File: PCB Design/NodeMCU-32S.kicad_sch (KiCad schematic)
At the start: 23 parts, among them J1 Screw_Terminal_01x02, J2 Screw_Terminal_01x02, J3 Screw_Terminal_01x02, J4 Screw_Terminal_01x02, J5 Screw_Terminal_01x03, J6 Screw_Terminal_01x02, Q1 IRLZ44N, Q2 2N2646, SW1 SW_DPDT_x2, U1 ESP32-DevKitC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

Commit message: Updated Photos and Voltage Divider
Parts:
- removed J6: Screw_Terminal_01x02, TerminalBlock:TerminalBlock_bornier-2_P5.08mm, symbol Connector:Screw_Terminal_01x02
- removed Q2: 2N2646, Package_TO_SOT_THT:TO-92L_Inline, symbol Transistor_BJT:2N2646
- removed R2: 270, Resistor_THT:R_Axial_DIN0207_L6.3mm_D2.5mm_P10.16mm_Horizontal, symbol Device:R_Small_US
- removed U3: S216S01, Package_SIP:SIP4_Sharp-SSR_P7.62mm_Straight, symbol Relay_SolidState:S216S01
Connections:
- net GND: now also SW1.3 (C)
- net at R3.2, SW1.1 (A): now also R4.1
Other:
- moved on the sheet: R4

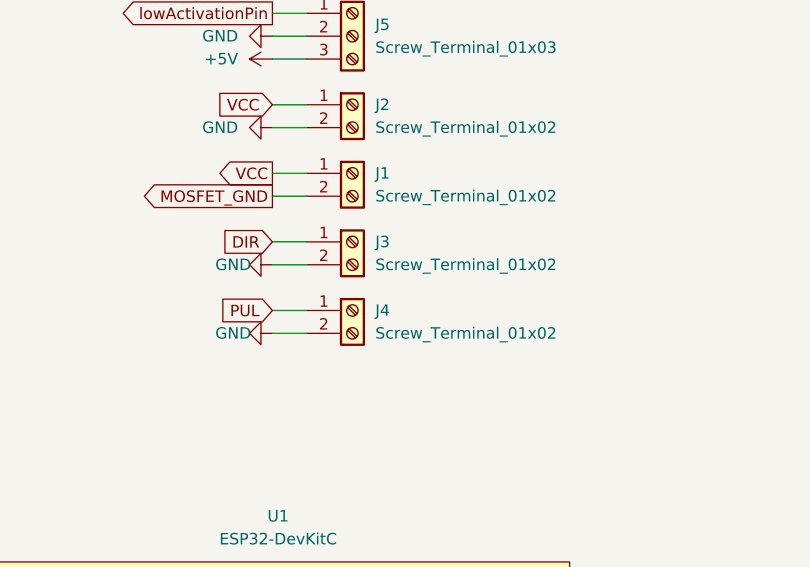
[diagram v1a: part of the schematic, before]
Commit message: PCB changes
Pluggable Stepper Motor
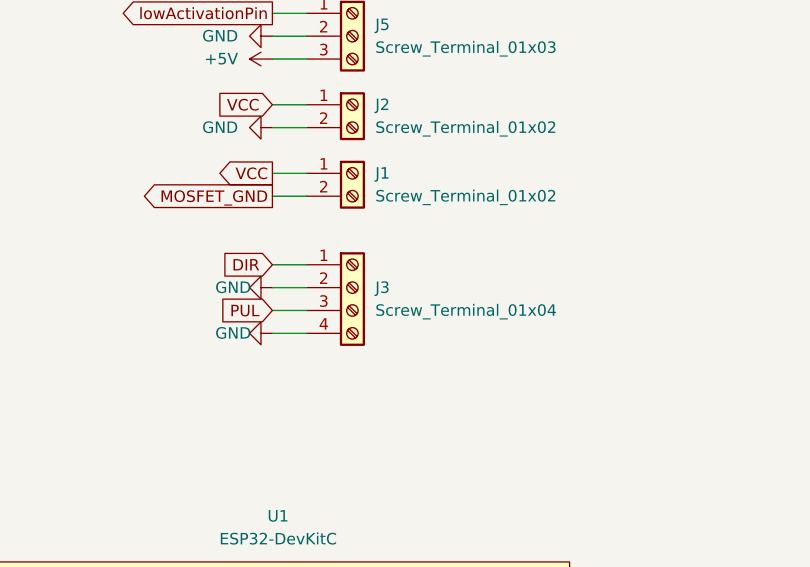
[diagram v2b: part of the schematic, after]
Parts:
- removed J3, J4: Screw_Terminal_01x02, TerminalBlock:TerminalBlock_bornier-2_P5.08mm, symbol Connector:Screw_Terminal_01x02
- added J3: Screw_Terminal_01x04, TerminalBlock:TerminalBlock_bornier-4_P5.08mm, symbol Connector:Screw_Terminal_01x04
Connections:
- net DIR: now also J3.1 (Pin_1)
- net GND: now also J3.2 (Pin_2), J3.4 (Pin_4)
- net PUL: now also J3.3 (Pin_3)
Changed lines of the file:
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@@
+    (stroke (width 0) (type default) (color 0 0 0 0))
+  )
+  (wire (pts (xy 140.97 64.77) (xy 144.78 64.77))
+    (stroke (width 0) (type default) (color 0 0 0 0))
+  )
+  (wire (pts (xy 200.66 109.22) (xy 205.74 109.22))
+    (stroke (width 0) (type default) (color 0 0 0 0))
+  )
+  (wire (pts (xy 270.51 72.39) (xy 266.7 72.39))
+    (stroke (width 0) (type default) (color 0 0 0 0))
+  )
+  (wire (pts (xy 140.97 69.85) (xy 144.78 69.85))
+    (stroke (width 0) (type default) (color 0 0 0 0))
+  )
+  (wire (pts (xy 99.06 144.78) (xy 100.33 144.78))
+    (stroke (width 0) (type default) (color 0 0 0 0))
+  )
+  (wire (pts (xy 262.89 39.37) (xy 262.89 41.91))
     (stroke (width 0) (type default) (color 0 0 0 0))
   )
   (wire (pts (xy 140.97 62.23) (xy 144.78 62.23))
-    (stroke (width 0) (type default) (color 0 0 0 0))
-  )
-  (wire (pts (xy 200.66 109.22) (xy 205.74 109.22))
-    (stroke (width 0) (type default) (color 0 0 0 0))
-  )
-  (wire (pts (xy 270.51 72.39) (xy 266.7 72.39))
-    (stroke (width 0) (type default) (color 0 0 0 0))
-  )
-  (wire (pts (xy 140.97 69.85) (xy 144.78 69.85))
-    (stroke (width 0) (type default) (color 0 0 0 0))
-  )
-  (wire (pts (xy 99.06 144.78) (xy 100.33 144.78))
-    (stroke (width 0) (type default) (color 0 0 0 0))
-  )
-  (wire (pts (xy 262.89 39.37) (xy 262.89 41.91))
-    (stroke (width 0) (type default) (color 0 0 0 0))
-  )
-  (wire (pts (xy 140.97 59.69) (xy 144.78 59.69))
     (stroke (width 0) (type default) (color 0 0 0 0))
   )
@@
     )
   )
-  (global_label "DIR" (shape input) (at 140.97 59.69 180) (fields_autoplaced)
-    (effects (font (size 1.27 1.27)) (justify right))
-    (property "Intersheet References" "${INTERSHEET_REFS}" (id 0) (at 135.4121 59.6106 0)
+  (global_label "DIR" (shape input) (at 140.97 62.23 180) (fields_autoplaced)
+    (effects (font (size 1.27 1.27)) (justify right))
+    (property "Intersheet References" "${INTERSHEET_REFS}" (id 0) (at 135.4121 62.1506 0)
       (effects (font (size 1.27 1.27)) (justify right) hide)
     )
@@
     (pin "6")
   )
-  (symbol (lib_id "Connector:Screw_Terminal_01x02") (at 149.86 59.69 0) (unit 1)
-    (in_bom yes) (on_board yes) (fields_autoplaced)
-    (property "Reference" "J3" (id 0) (at 152.4 59.6899 0)
-      (effects (font (size 1.27 1.27)) (justify left))
-    )
-    (property "Value" "Screw_Terminal_01x02" (id 1) (at 152.4 62.2299 0)
-      (effects (font (size 1.27 1.27)) (justify left))
-    )
-    (property "Footprint" "TerminalBlock:TerminalBlock_bornier-2_P5.08mm" (id 2) (at 149.86 59.69 0)
-      (effects (font (size 1.27 1.27)) hide)
-    )
-    (property "Datasheet" "~" (id 3) (at 149.86 59.69 0)
-      (effects (font (size 1.27 1.27)) hide)
-    )
-    (pin "1")
-    (pin "2")
-  )
   (symbol (lib_id "Device:R_US") (at 198.12 121.92 270) (unit 1)
     (in_bom yes) (on_board yes) (fields_autoplaced)
@@
   (symbol (lib_id "power:GND") (at 205.74 109.22 90) (unit 1)
     (in_bom yes) (on_board yes) (fields_autoplaced)
-    (property "Reference" "#PWR?" (id 0) (at 212.09 109.22 0)
+    (property "Reference" "#PWR01" (id 0) (at 212.09 109.22 0)
       (effects (font (size 1.27 1.27)) hide)
     )
@@
     (pin "1")
   )
-  (symbol (lib_id "Connector:Screw_Terminal_01x02") (at 149.86 67.31 0) (unit 1)
-    (in_bom yes) (on_board yes) (fields_autoplaced)
-    (property "Reference" "J4" (id 0) (at 152.4 67.3099 0)
-      (effects (font (size 1.27 1.27)) (justify left))
-    )
-    (property "Value" "Screw_Terminal_01x02" (id 1) (at 152.4 69.8499 0)
-      (effects (font (size 1.27 1.27)) (justify left))
-    )
-    (property "Footprint" "TerminalBlock:TerminalBlock_bornier-2_P5.08mm" (id 2) (at 149.86 67.31 0)
-      (effects (font (size 1.27 1.27)) hide)
-    )
-    (property "Datasheet" "~" (id 3) (at 149.86 67.31 0)
-      (effects (font (size 1.27 1.27)) hide)
-    )
-    (pin "1")
-    (pin "2")
-  )
-  (symbol (lib_id "power:GND") (at 140.97 62.23 270) (mirror x) (unit 1)
+  (symbol (lib_id "power:GND") (at 140.97 64.77 270) (mirror x) (unit 1)
     (in_bom yes) (on_board yes)
-    (property "Reference" "#PWR0104" (id 0) (at 134.62 62.23 0)
-      (effects (font (size 1.27 1.27)) hide)
-    )
-    (property "Value" "GND" (id 1) (at 134.62 62.23 90)
-      (effects (font (size 1.27 1.27)) (justify left))
-    )
-    (property "Footprint" "" (id 2) (at 140.97 62.23 0)
-      (effects (font (size 1.27 1.27)) hide)
-    )
-    (property "Datasheet" "" (id 3) (at 140.97 62.23 0)
+    (property "Reference" "#PWR0104" (id 0) (at 134.62 64.77 0)
+      (effects (font (size 1.27 1.27)) hide)
+    )
+    (property "Value" "GND" (id 1) (at 134.62 64.77 90)
+      (effects (font (size 1.27 1.27)) (justify left))
+    )
+    (property "Footprint" "" (id 2) (at 140.97 64.77 0)
+      (effects (font (size 1.27 1.27)) hide)
+    )
+    (property "Datasheet" "" (id 3) (at 140.97 64.77 0)
       (effects (font (size 1.27 1.27)) hide)
     )
@@
     (pin "2")
   )
+  (symbol (lib_id "Connector:Screw_Terminal_01x04") (at 149.86 64.77 0) (unit 1)
+    (in_bom yes) (on_board yes) (fields_autoplaced)
+    (property "Reference" "J3" (id 0) (at 152.4 64.7699 0)
+      (effects (font (size 1.27 1.27)) (justify left))
+    )
+    (property "Value" "Screw_Terminal_01x04" (id 1) (at 152.4 67.3099 0)
+      (effects (font (size 1.27 1.27)) (justify left))
+    )
+    (property "Footprint" "TerminalBlock:TerminalBlock_bornier-4_P5.08mm" (id 2) (at 149.86 64.77 0)
+      (effects (font (size 1.27 1.27)) hide)
+    )
+    (property "Datasheet" "~" (id 3) (at 149.86 64.77 0)
+      (effects (font (size 1.27 1.27)) hide)
+    )
+    (pin "1")
+    (pin "2")
+    (pin "3")
+    (pin "4")
+  )
   (symbol (lib_id "power:+5V") (at 204.47 121.92 270) (unit 1)
     (in_bom yes) (on_board yes) (fields_autoplaced)
@@
   )
   (symbol_instances
+    (path "/398158d8-f37b-482f-8cfa-1524e445a192"
+      (reference "#PWR01") (unit 1) (value "GND") (footprint "")
+    )
     (path "/2c3dc467-cd0c-4dfc-a507-951e5fe27b94"
       (reference "#PWR02") (unit 1) (value "GND") (footprint "")
@@
       (reference "#PWR0113") (unit 1) (value "+3.3V") (footprint "")
     )
-    (path "/398158d8-f37b-482f-8cfa-1524e445a192"
-      (reference "#PWR?") (unit 1) (value "GND") (footprint "")
-    )
     (path "/414d8815-2cd5-4a60-a6c9-452c5087ded6"
       (reference "C1") (unit 1) (value "C_Polarized_Small_US") (footprint "Capacitor_THT:CP_Radial_D8.0mm_P3.80mm")
@@
       (reference "J2") (unit 1) (value "Screw_Terminal_01x02") (footprint "TerminalBlock:TerminalBlock_bornier-2_P5.08mm")
     )
-    (path "/11bb7bd3-e3b3-4a90-8de5-c47f1c02004b"
-      (reference "J3") (unit 1) (value "Screw_Terminal_01x02") (footprint "TerminalBlock:TerminalBlock_bornier-2_P5.08mm")
-    )
-    (path "/9c843d3f-6a97-4710-b259-032a83bd2105"
-      (reference "J4") (unit 1) (value "Screw_Terminal_01x02") (footprint "TerminalBlock:TerminalBlock_bornier-2_P5.08mm")
+    (path "/d2f66f9d-5757-4777-9b5b-ffa8e9f9e173"
+      (reference "J3") (unit 1) (value "Screw_Terminal_01x04") (footprint "TerminalBlock:TerminalBlock_bornier-4_P5.08mm")
     )
     (path "/6982722a-cf78-48a8-9760-9f79c938704a"
